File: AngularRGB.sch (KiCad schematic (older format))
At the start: 4 parts

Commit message: MCU Connections
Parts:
- added C? (x3): 100n, symbol pspice:CAP
- added R? (x2): 5k1, symbol Device:R
- added SW?: SW_Push, symbol Switch:SW_Push
- C?: value CAP -> 100n
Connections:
- net GND: now also C?.2, U?.15 (GND), U?.23 (GND), U?.35 (GND), U?.43 (GND), U?.45 (GND), U?.5 (UGND), C?.2, C?.2, C?.2, R?.2, SW?.1
- net VCC: now also C?.1, C?.1, C?.1, C?.1, R?.1
- net at U?.13 (~RESET): now also R?.2, SW?.2
- net XTAL2: now reaches U?.16 (XTAL2)
- net XTAL1: now reaches U?.17 (XTAL1)
- net at U?.33 (~HWB~/PE2): now also R?.1
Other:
- note added: "MCU Decoupling"
- note added: "MCU\n"
- moved on the sheet: C?, U?

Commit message: USB Sch
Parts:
- added F?: Fuse, symbol Device:Fuse
- added J?: USB_C_Receptacle_USB2.0, symbol Connector:USB_C_Receptacle_USB2.0
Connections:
- net GND: now also J?.A1 (GND), J?.A12 (GND), J?.B1 (GND), J?.B12 (GND), J?.S1 (SHIELD)
- net VCC: now also F?.1
- new net: F?.2, J?.A4 (VBUS), J?.A9 (VBUS), J?.B4 (VBUS), J?.B9 (VBUS)
- new net: J?.A6 (D+), J?.B6 (D+)
- new net: J?.A7 (D-), J?.B7 (D-)
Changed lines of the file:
@@
 Text Notes 800  6750 2    50   ~ 0
 MCU\n
+$Comp
+L Connector:USB_C_Receptacle_USB2.0 J?
+U 1 1 5CB6AAC4
+P 5050 1500
+F 0 "J?" H 4700 2350 50  0000 C CNN
+F 1 "USB_C_Receptacle_USB2.0" H 4950 2250 50  0000 C CNN
+F 2 "" H 5200 1500 50  0001 C CNN
+F 3 "https://www.usb.org/sites/default/files/documents/usb_type-c.zip" H 5200 1500 50  0001 C CNN
+	1    5050 1500
+	1    0    0    -1
+$EndComp
+$Comp
+L power:VCC #PWR?
+U 1 1 5CB6B5D1
+P 6050 800
+F 0 "#PWR?" H 6050 650 50  0001 C CNN
+F 1 "VCC" H 6067 973 50  0000 C CNN
+F 2 "" H 6050 800 50  0001 C CNN
+F 3 "" H 6050 800 50  0001 C CNN
+	1    6050 800
+	1    0    0    -1
+$EndComp
+Wire Wire Line
+	5650 1400 5650 1500
+Wire Wire Line
+	5650 1600 5650 1700
+$Comp
+L Device:Fuse F?
+U 1 1 5CB6C649
+P 5800 900
+F 0 "F?" V 5603 900 50  0000 C CNN
+F 1 "Fuse" V 5694 900 50  0000 C CNN
+F 2 "" V 5730 900 50  0001 C CNN
+F 3 "~" H 5800 900 50  0001 C CNN
+	1    5800 900
+	0    1    1    0
+$EndComp
+Wire Wire Line
+	4900 2400 5050 2400
+Wire Wire Line
+	4750 2400 4900 2400
+Connection ~ 4900 2400
+Wire Wire Line
+	4900 2500 4900 2400
+$Comp
+L power:GND #PWR?
+U 1 1 5CB6B180
+P 4900 2500
+F 0 "#PWR?" H 4900 2250 50  0001 C CNN
+F 1 "GND" H 4905 2327 50  0000 C CNN
+F 2 "" H 4900 2500 50  0001 C CNN
+F 3 "" H 4900 2500 50  0001 C CNN
+	1    4900 2500
+	1    0    0    -1
+$EndComp
+Wire Wire Line
+	5950 900  6050 900
+Wire Wire Line
+	6050 900  6050 800
 $EndSCHEMATC

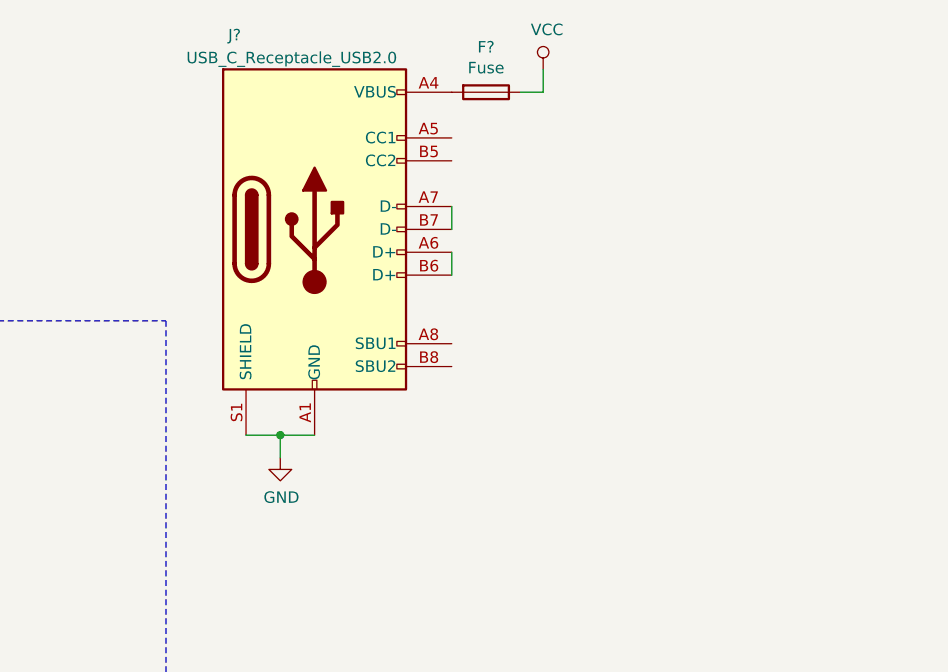
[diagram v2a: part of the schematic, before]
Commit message: USB Port
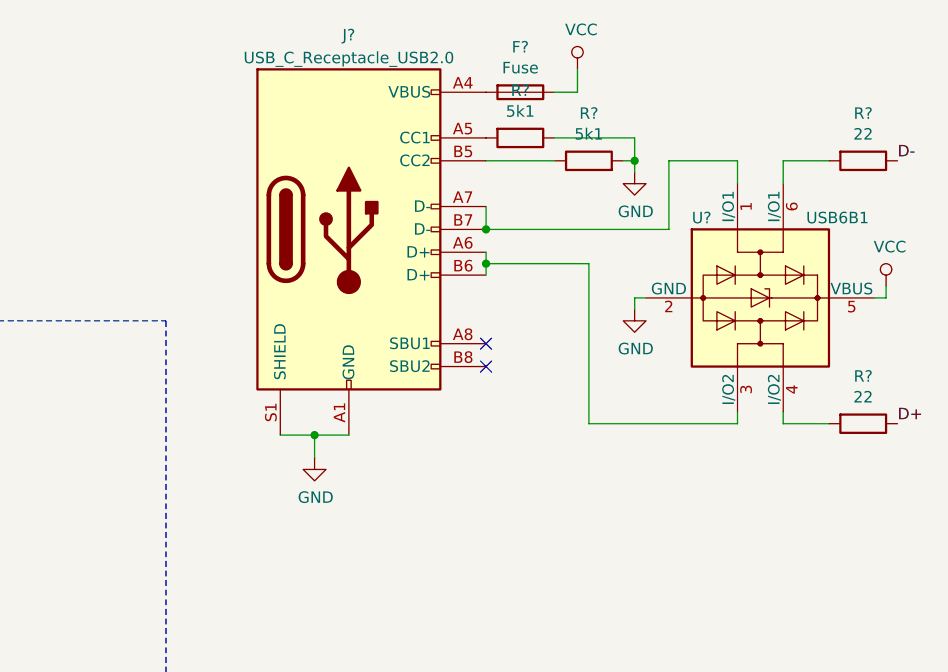
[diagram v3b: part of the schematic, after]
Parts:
- added R? (x2): 5k1, symbol Device:R
- added R? (x2): 22, symbol Device:R
- added U?: USB6B1, Package_SO:SOIC-8_3.9x4.9mm_P1.27mm, symbol Power_Protection:USB6B1
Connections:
- net D+: now also R?.1
- net D-: now also R?.1
- net GND: now also R?.1, R?.2, U?.2 (GND)
- net VCC: now also U?.5 (VBUS)
- net at J?.A5 (CC1): now also R?.2
- net at J?.A6 (D+), J?.B6 (D+): now also U?.3 (I/O2)
- net at J?.A7 (D-), J?.B7 (D-): now also U?.1 (I/O1)
- net at J?.B5 (CC2): now also R?.1
- new net: R?.2, U?.4 (I/O2)
- new net: R?.2, U?.6 (I/O1)
- no-connect marks 1 -> 3
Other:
- moved on the sheet: F?, J?
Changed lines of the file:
@@
 EESchema Schematic File Version 4
 LIBS:AngularRGB-cache
-EELAYER 26 0
+EELAYER 29 0
 EELAYER END
 $Descr A4 11693 8268
@@
 L Connector:USB_C_Receptacle_USB2.0 J?
 U 1 1 5CB6AAC4
-P 5050 1500
-F 0 "J?" H 4700 2350 50  0000 C CNN
-F 1 "USB_C_Receptacle_USB2.0" H 4950 2250 50  0000 C CNN
-F 2 "" H 5200 1500 50  0001 C CNN
-F 3 "https://www.usb.org/sites/default/files/documents/usb_type-c.zip" H 5200 1500 50  0001 C CNN
-	1    5050 1500
+P 5200 1500
+F 0 "J?" H 5200 2350 50  0000 C CNN
+F 1 "USB_C_Receptacle_USB2.0" H 5200 2250 50  0000 C CNN
+F 2 "" H 5350 1500 50  0001 C CNN
+F 3 "https://www.usb.org/sites/default/files/documents/usb_type-c.zip" H 5350 1500 50  0001 C CNN
+	1    5200 1500
 	1    0    0    -1
 $EndComp
@@
 L power:VCC #PWR?
 U 1 1 5CB6B5D1
-P 6050 800
-F 0 "#PWR?" H 6050 650 50  0001 C CNN
-F 1 "VCC" H 6067 973 50  0000 C CNN
-F 2 "" H 6050 800 50  0001 C CNN
-F 3 "" H 6050 800 50  0001 C CNN
-	1    6050 800
-	1    0    0    -1
-$EndComp
-Wire Wire Line
-	5650 1400 5650 1500
-Wire Wire Line
-	5650 1600 5650 1700
+P 6200 800
+F 0 "#PWR?" H 6200 650 50  0001 C CNN
+F 1 "VCC" H 6217 973 50  0000 C CNN
+F 2 "" H 6200 800 50  0001 C CNN
+F 3 "" H 6200 800 50  0001 C CNN
+	1    6200 800
+	1    0    0    -1
+$EndComp
+Wire Wire Line
+	5800 1400 5800 1500
+Wire Wire Line
+	5800 1600 5800 1650
 $Comp
 L Device:Fuse F?
 U 1 1 5CB6C649
-P 5800 900
-F 0 "F?" V 5603 900 50  0000 C CNN
-F 1 "Fuse" V 5694 900 50  0000 C CNN
-F 2 "" V 5730 900 50  0001 C CNN
-F 3 "~" H 5800 900 50  0001 C CNN
-	1    5800 900
+P 5950 900
+F 0 "F?" V 5753 900 50  0000 C CNN
+F 1 "Fuse" V 5844 900 50  0000 C CNN
+F 2 "" V 5880 900 50  0001 C CNN
+F 3 "~" H 5950 900 50  0001 C CNN
+	1    5950 900
 	0    1    1    0
 $EndComp
 Wire Wire Line
+	5050 2400 5200 2400
+Wire Wire Line
 	4900 2400 5050 2400
-Wire Wire Line
-	4750 2400 4900 2400
-Connection ~ 4900 2400
-Wire Wire Line
-	4900 2500 4900 2400
+Connection ~ 5050 2400
+Wire Wire Line
+	5050 2500 5050 2400
 $Comp
 L power:GND #PWR?
 U 1 1 5CB6B180
-P 4900 2500
-F 0 "#PWR?" H 4900 2250 50  0001 C CNN
-F 1 "GND" H 4905 2327 50  0000 C CNN
-F 2 "" H 4900 2500 50  0001 C CNN
-F 3 "" H 4900 2500 50  0001 C CNN
-	1    4900 2500
-	1    0    0    -1
-$EndComp
-Wire Wire Line
-	5950 900  6050 900
-Wire Wire Line
-	6050 900  6050 800
+P 5050 2500
+F 0 "#PWR?" H 5050 2250 50  0001 C CNN
+F 1 "GND" H 5055 2327 50  0000 C CNN
+F 2 "" H 5050 2500 50  0001 C CNN
+F 3 "" H 5050 2500 50  0001 C CNN
+	1    5050 2500
+	1    0    0    -1
+$EndComp
+Wire Wire Line
+	6100 900  6200 900
+Wire Wire Line
+	6200 900  6200 800
+NoConn ~ 5800 2000
+NoConn ~ 5800 2100
+$Comp
+L power:GND #PWR?
+U 1 1 5CB78A38
+P 6450 1250
+F 0 "#PWR?" H 6450 1000 50  0001 C CNN
+F 1 "GND" H 6455 1077 50  0000 C CNN
+F 2 "" H 6450 1250 50  0001 C CNN
+F 3 "" H 6450 1250 50  0001 C CNN
+	1    6450 1250
+	1    0    0    -1
+$EndComp
+$Comp
+L Device:R R?
+U 1 1 5CB7A006
+P 5950 1100
+F 0 "R?" V 5743 1100 50  0000 C CNN
+F 1 "5k1" V 5834 1100 50  0000 C CNN
+F 2 "" V 5880 1100 50  0001 C CNN
+F 3 "~" H 5950 1100 50  0001 C CNN
+	1    5950 1100
+	0    1    1    0
+$EndComp
+$Comp
+L Device:R R?
+U 1 1 5CB7AB72
+P 6250 1200
+F 0 "R?" V 6457 1200 50  0000 C CNN
+F 1 "5k1" V 6366 1200 50  0000 C CNN
+F 2 "" V 6180 1200 50  0001 C CNN
+F 3 "~" H 6250 1200 50  0001 C CNN
+	1    6250 1200
+	0    -1   -1   0
+$EndComp
+Wire Wire Line
+	6100 1200 5800 1200
+Wire Wire Line
+	6400 1200 6450 1200
+Wire Wire Line
+	6450 1200 6450 1250
+Wire Wire Line
+	6450 1200 6450 1100
+Wire Wire Line
+	6450 1100 6100 1100
+Connection ~ 6450 1200
+$Comp
+L power:GND #PWR?
+U 1 1 5CB8AE03
+P 6450 1850
+F 0 "#PWR?" H 6450 1600 50  0001 C CNN
+F 1 "GND" H 6455 1677 50  0000 C CNN
+F 2 "" H 6450 1850 50  0001 C CNN
+F 3 "" H 6450 1850 50  0001 C CNN
+	1    6450 1850
+	1    0    0    -1
+$EndComp
+$Comp
+L power:VCC #PWR?
+U 1 1 5CB8B7A3
+P 7550 1750
+F 0 "#PWR?" H 7550 1600 50  0001 C CNN
+F 1 "VCC" H 7567 1923 50  0000 C CNN
+F 2 "" H 7550 1750 50  0001 C CNN
+F 3 "" H 7550 1750 50  0001 C CNN
+	1    7550 1750
+	1    0    0    -1
+$EndComp
+Wire Wire Line
+	7550 1750 7550 1800
+Wire Wire Line
+	7550 1800 7500 1800
+Wire Wire Line
+	6500 1800 6450 1800
+Wire Wire Line
+	6450 1800 6450 1850
+Wire Wire Line
+	5800 1500 6600 1500
+Wire Wire Line
+	6600 1500 6600 1200
+Wire Wire Line
+	6600 1200 6900 1200
+Wire Wire Line
+	6900 1200 6900 1300
+Connection ~ 5800 1500
+Wire Wire Line
+	5800 1650 6250 1650
+Wire Wire Line
+	6250 1650 6250 2350
+Wire Wire Line
+	6250 2350 6900 2350
+Wire Wire Line
+	6900 2350 6900 2300
+Connection ~ 5800 1650
+Wire Wire Line
+	5800 1650 5800 1700
+Wire Wire Line
+	7100 1300 7100 1200
+Wire Wire Line
+	7100 1200 7300 1200
+Wire Wire Line
+	7100 2300 7100 2350
+Wire Wire Line
+	7100 2350 7300 2350
+Text Label 7600 1200 0    50   ~ 0
+D-
+Text Label 7600 2350 0    50   ~ 0
+D+
+$Comp
+L Power_Protection:USB6B1 U?
+U 1 1 5CB7FD9E
+P 7000 1800
+F 0 "U?" V 6650 1500 50  0000 L CNN
+F 1 "USB6B1" V 6650 2000 50  0000 L CNN
+F 2 "Package_SO:SOIC-8_3.9x4.9mm_P1.27mm" H 6025 1400 50  0001 C CNN
+F 3 "http://www.st.com/content/ccc/resource/technical/document/datasheet/3e/ec/b2/54/b2/76/47/90/CD00001361.pdf/files/CD00001361.pdf/jcr:content/translations/en.CD00001361.pdf" H 6050 1700 50  0001 C CNN
+	1    7000 1800
+	0    1    1    0
+$EndComp
+$Comp
+L Device:R R?
+U 1 1 5CB931C6
+P 7450 1200
+F 0 "R?" V 7243 1200 50  0000 C CNN
+F 1 "22" V 7334 1200 50  0000 C CNN
+F 2 "" V 7380 1200 50  0001 C CNN
+F 3 "~" H 7450 1200 50  0001 C CNN
+	1    7450 1200
+	0    1    1    0
+$EndComp
+$Comp
+L Device:R R?
+U 1 1 5CB93921
+P 7450 2350
+F 0 "R?" V 7243 2350 50  0000 C CNN
+F 1 "22" V 7334 2350 50  0000 C CNN
+F 2 "" V 7380 2350 50  0001 C CNN
+F 3 "~" H 7450 2350 50  0001 C CNN
+	1    7450 2350
+	0    1    1    0
+$EndComp
 $EndSCHEMATC

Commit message: Matrix Layout
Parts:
- added SW1.25U? (x6): MX_1.25U, symbol MX_Switches:MX_1.25U
- added SW1.75U? (x2): MX_1.75U, symbol MX_Switches:MX_1.75U
- added SW2.25U?: MX_2.25U, symbol MX_Switches:MX_2.25U
- added SW2.75U?: MX_2.75U, symbol MX_Switches:MX_2.75U
- added SW? (x31): MX_1U, symbol MX_Switches:MX_1U

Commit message: Annotation
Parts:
- added C2, C3: 20pF, symbol Device:C
- added D1, D10, D11, D12, D13, D14, D15, D16, D17, D18, D19, D2, D20, D21, D22, D23, D24, D25, D26, D27, D28, D29, D3, D30, D31, D32, D33, D34, D35, D36, D37, D38, D39, D4, D40, D41, D5, D6, D7, D8, D9: D, symbol Device:D
- added Y1: Crystal_GND24, symbol Device:Crystal_GND24
- gave numbers to parts that had none: 58
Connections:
- net GND: now also C2.2, C3.2, Y1.2, Y1.4
- net XTAL1: now also C2.1, Y1.1
- net XTAL2: now also C3.1, Y1.3
- net R0: now reaches SW2.1
- net R0: now also SW12.1, SW14.1, SW17.1, SW20.1, SW23.1, SW26.1, SW29.1, SW3.1, SW31.1, SW6.1, SW9.1
- net at SW2.2: now also D1.2 (A)
- net at SW3.2: now also D5.2 (A)
- net R1: now reaches SW4.1
- net R1: now also SW1.25U1.1, SW1.75U2.1, SW10.1, SW13.1, SW15.1, SW18.1, SW21.1, SW24.1, SW27.1, SW7.1
- net at SW4.2: now also D6.2 (A)
- net R3: now reaches SW5.1
- net R3: now also SW1.25U2.1, SW1.25U3.1, SW1.25U4.1, SW1.25U6.1, SW2.25U1.1, SW2.75U1.1, SW30.1
- net at SW5.2: now also D7.2 (A)
- net at SW6.2: now also D8.2 (A)
- net at SW7.2: now also D9.2 (A)
- net R2: now reaches SW8.1
- net R2: now also SW1.25U5.1, SW1.75U1.1, SW11.1, SW16.1, SW19.1, SW22.1, SW25.1, SW28.1, SW32.1
- net at SW8.2: now also D10.2 (A)
- net at SW9.2: now also D12.2 (A)
- net at SW10.2: now also D13.2 (A)
- net at SW11.2: now also D14.2 (A)
- net at SW12.2: now also D15.2 (A)
- net at SW13.2: now also D16.2 (A)
- net at SW14.2: now also D18.2 (A)
- net at SW15.2: now also D19.2 (A)
- net at SW16.2: now also D20.2 (A)
- net at SW17.2: now also D21.2 (A)
- net at SW18.2: now also D22.2 (A)
- net at SW19.2: now also D23.2 (A)
- net at SW20.2: now also D24.2 (A)
- net at SW21.2: now also D25.2 (A)
- net at SW22.2: now also D26.2 (A)
- net at SW23.2: now also D28.2 (A)
- net at SW24.2: now also D29.2 (A)
- net at SW25.2: now also D30.2 (A)
- net at SW26.2: now also D31.2 (A)
- net at SW27.2: now also D32.2 (A)
- net at SW28.2: now also D33.2 (A)
- net at SW29.2: now also D35.2 (A)
- net at SW30.2: now also D37.2 (A)
- net at SW31.2: now also D38.2 (A)
- net at SW32.2: now also D40.2 (A)
- net at SW1.25U1.2: now also D2.2 (A)
- net at SW1.75U1.2: now also D3.2 (A)
- net at SW1.25U2.2: now also D4.2 (A)
- net at SW1.25U3.2: now also D11.2 (A)
- net at SW1.25U4.2: now also D34.2 (A)
- net at SW1.25U6.2: now also D41.2 (A)
- net at SW1.25U5.2: now also D36.2 (A)
- net at SW1.75U2.2: now also D39.2 (A)
- net at SW2.25U1.2: now also D27.2 (A)
- net at SW2.75U1.2: now also D17.2 (A)
- new net C0: D1.1 (K), D2.1 (K), D3.1 (K), D4.1 (K)
- new net C1: D5.1 (K), D6.1 (K), D7.1 (K)
- new net C10: D35.1 (K), D36.1 (K), D37.1 (K)
- new net C11: D38.1 (K), D39.1 (K), D40.1 (K), D41.1 (K)
- new net C2: D10.1 (K), D11.1 (K), D8.1 (K), D9.1 (K)
- new net C3: D12.1 (K), D13.1 (K), D14.1 (K)
- new net C4: D15.1 (K), D16.1 (K), D17.1 (K)
- new net C5: D18.1 (K), D19.1 (K), D20.1 (K)
- new net C6: D21.1 (K), D22.1 (K), D23.1 (K)
- new net C7: D24.1 (K), D25.1 (K), D26.1 (K), D27.1 (K)
- new net C8: D28.1 (K), D29.1 (K), D30.1 (K)
- new net C9: D31.1 (K), D32.1 (K), D33.1 (K), D34.1 (K)
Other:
- moved on the sheet: R2, SW1.25U1, SW1.25U2, SW1.25U3, SW1.25U4, SW1.25U5, SW1.25U6, SW1.75U1, SW1.75U2, SW10, SW11, SW12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

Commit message: Footprint Linking
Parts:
- C1, C2, C3, C4, C5, C6, C7, C8: footprint (none) -> Capacitor_SMD:C_0603_1608Metric
- D1: footprint (none) -> Diode_SMD:D_SOD-123F
- D10, D11, D12, D13, D14, D15, D16, D17, D18, D19, D2, D20, D21, D22, D23, D24, D25, D26, D27, D28, D29, D3, D30, D31, D32, D33, D34, D35, D36, D37, D38, D39, D4, D40, D41, D5, D6, D7, D8, D9: footprint (none) -> Diode_SMD:D_SOD-123
- F1: footprint (none) -> Fuse:Fuse_0603_1608Metric
- J1: footprint (none) -> Type-C:HRO-TYPE-C-31-M-12-Assembly
- R1, R2, R3, R4, R5, R6: footprint (none) -> Resistor_SMD:R_0603_1608Metric
- SW1: footprint (none) -> Button_Switch_THT:SW_PUSH_6mm
- SW1.25U1, SW1.25U2, SW1.25U3, SW1.25U4, SW1.25U5, SW1.25U6: footprint (none) -> MX_Switches:MX_1.25U
- SW1.75U1, SW1.75U2: footprint (none) -> MX_Switches:MX-1.75U
- SW10, SW11, SW12, SW13, SW14, SW15, SW16, SW17, SW18, SW19, SW2, SW20, SW21, SW22, SW23, SW24, SW25, SW26, SW27, SW28, SW29, SW3, SW30, SW31, SW32, SW4, SW5, SW6, SW7, SW8, SW9: footprint (none) -> MX_Switches:MX-1U
- SW2.25U1, SW2.75U1: footprint (none) -> MX_Switches:MX-2.75U
- U2: footprint Package_SO:SOIC-8_3.9x4.9mm_P1.27mm -> Package_TO_SOT_SMD:SOT-23-6
- Y1: footprint (none) -> Crystal:Crystal_SMD_3225-4Pin_3.2x2.5mm

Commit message: Layout
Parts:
- removed J1: USB_C_Receptacle_USB2.0, Type-C:HRO-TYPE-C-31-M-12-Assembly, symbol Connector:USB_C_Receptacle_USB2.0
- added D42: D, Diode_SMD:D_SOD-123, symbol Device:D
- added H1, H10, H2, H3, H4, H5, H6, H7, H8, H9: MountingHole_Pad, MountingHole:MountingHole_2.2mm_M2_DIN965_Pad, symbol Mechanical:MountingHole_Pad
- added SW33: MX_1U, MX_Switches:MX-1U, symbol AngularRGB-rescue:MX_1U-MX_Switches
- added USB1: HRO-TYPE-C-31-M-12, Type-C:HRO-TYPE-C-31-M-12-Assembly, symbol Type-C:HRO-TYPE-C-31-M-12
- SW1: footprint Button_Switch_THT:SW_PUSH_6mm -> MX_Switches:SPST-NO-4
- SW1.25U1, SW1.25U2, SW1.25U3, SW1.25U4, SW1.25U5, SW1.25U6: symbol MX_Switches:MX_1.25U -> AngularRGB-rescue:MX_1.25U-MX_Switches
- SW1.75U1, SW1.75U2: symbol MX_Switches:MX_1.75U -> AngularRGB-rescue:MX_1.75U-MX_Switches
- SW10, SW11, SW12, SW13, SW14, SW15, SW16, SW17, SW18, SW19, SW2, SW20, SW21, SW22, SW23, SW24, SW25, SW26, SW27, SW28, SW29, SW3, SW30, SW31, SW32, SW4, SW5, SW6, SW7, SW8, SW9: symbol MX_Switches:MX_1U -> AngularRGB-rescue:MX_1U-MX_Switches
- SW2.25U1: footprint MX_Switches:MX-2.75U -> MX_Switches:MX-2.25U; symbol MX_Switches:MX_2.25U -> AngularRGB-rescue:MX_2.25U-MX_Switches
- SW2.75U1: symbol MX_Switches:MX_2.75U -> AngularRGB-rescue:MX_2.75U-MX_Switches
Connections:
- net C4: now also D42.1 (K)
- net D+: now also R5.1; no longer R6.1
- net D-: now also R6.1; no longer R5.1
- net GND: now also H1.1, H10.1, H2.1, H3.1, H4.1, H5.1, H6.1, H7.1, H8.1, H9.1, USB1.1 (GND), USB1.12 (GND), USB1.13 (SHIELD)
- net R2: now also SW33.1
- net VCC: no longer U2.5 (VBUS)
- net UCAP: now reaches C5.1, U1.6 (UCAP)
- net VBUS: now reaches F1.2
- net VBUS: now also U2.5 (VBUS), USB1.11 (VBUS), USB1.2 (VBUS)
- net at R3.2: now also USB1.4 (CC1)
- net at U2.3 (I/O2): now also R6.2
- net at U2.1 (I/O1): now also R5.2
- net at R4.1: now also USB1.10 (CC2)
- net DN_PRE: now reaches U2.4 (I/O2)
- net DN_PRE: now also USB1.5 (DN2), USB1.7 (DN1); no longer R6.2
- net DP_PRE: now reaches U2.6 (I/O1)
- net DP_PRE: now also USB1.6 (DP1), USB1.8 (DP2); no longer R5.2
- new net: D42.2 (A), SW33.2
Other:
- moved on the sheet: F1, R3, R4, R5, R6, U2

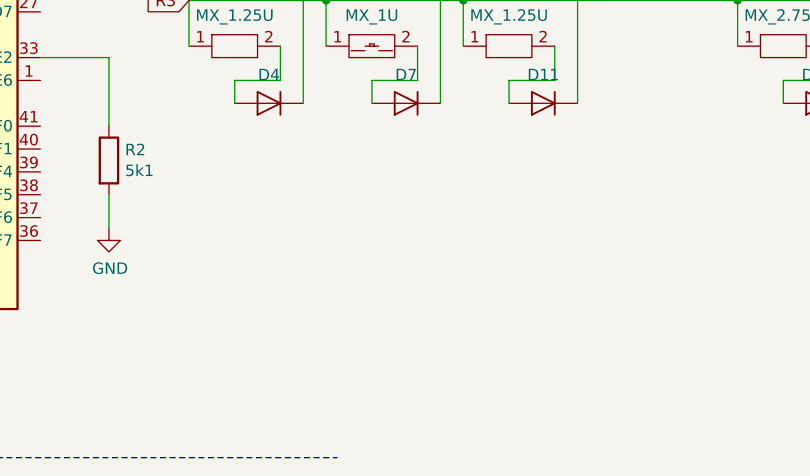
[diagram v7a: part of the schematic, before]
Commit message: WS2812B-Mini Symbole
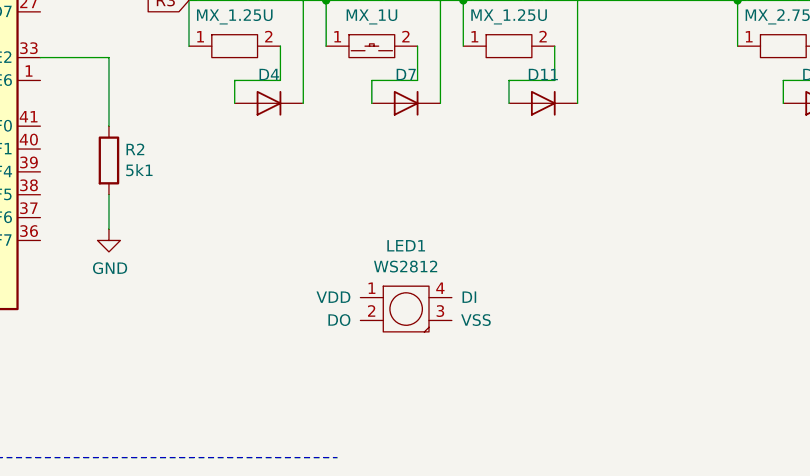
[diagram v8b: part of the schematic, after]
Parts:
- added LED1: WS2812, symbol MX_Switches:WS2812
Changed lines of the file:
@@
 Wire Wire Line
 	8200 2200 8450 2200
+$Comp
+L MX_Switches:WS2812 LED1
+U 1 1 5CD98066
+P 4700 6150
+F 0 "LED1" H 4700 6425 50  0000 C CNN
+F 1 "WS2812" H 4700 6334 50  0000 C CNN
+F 2 "" H 4700 6150 50  0001 C CNN
+F 3 "" H 4700 6150 50  0001 C CNN
+	1    4700 6150
+	1    0    0    -1
+$EndComp
 $EndSCHEMATC
